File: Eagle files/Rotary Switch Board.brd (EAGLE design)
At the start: 25.4 x 25.4 mm, 0 parts

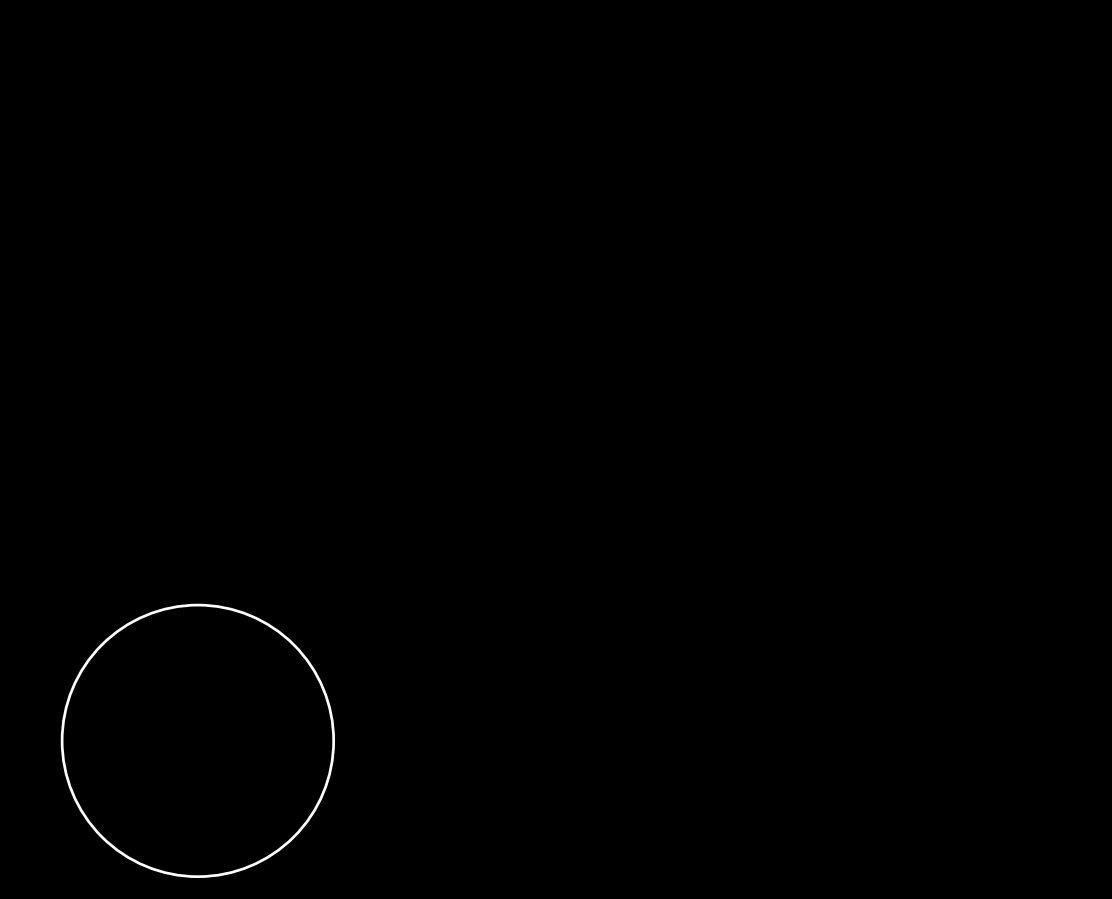
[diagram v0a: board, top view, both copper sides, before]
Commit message: Removed Rotary switch board file
Not working with OSHpark. Will troubleshoot later.
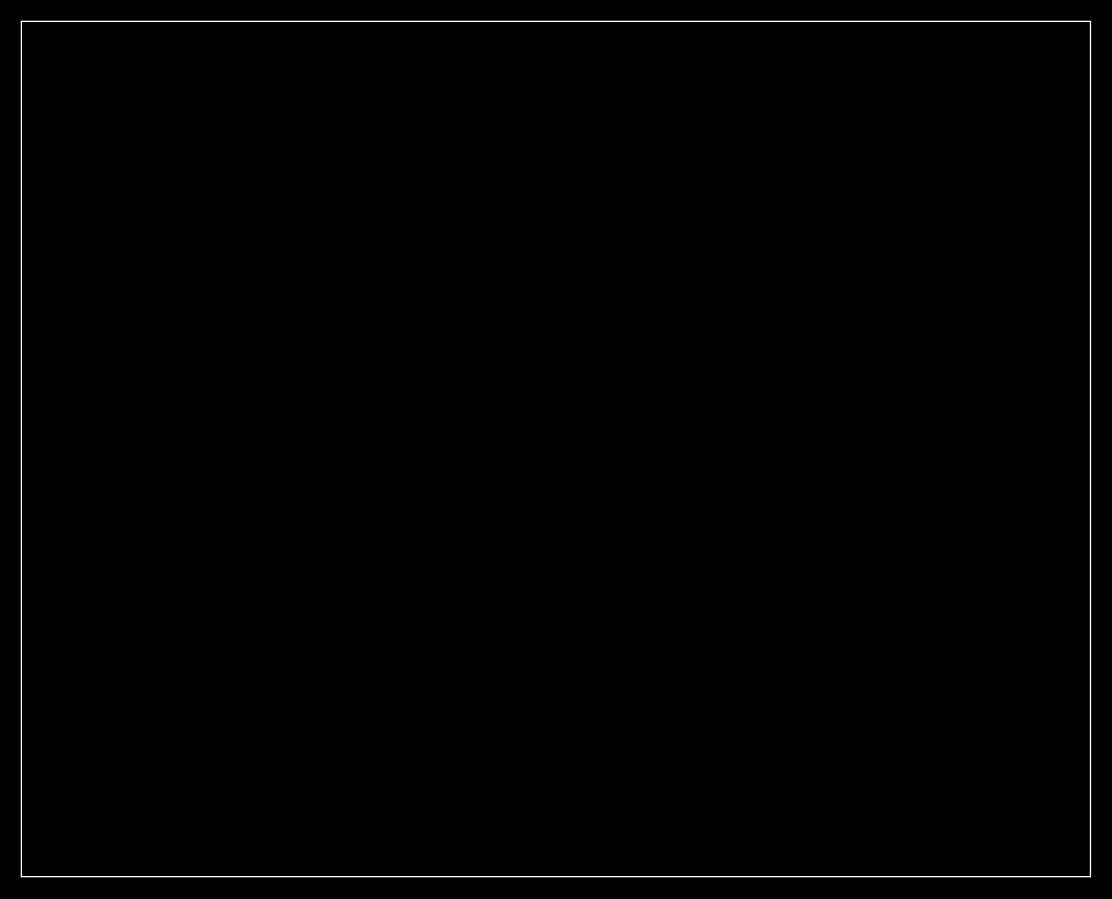
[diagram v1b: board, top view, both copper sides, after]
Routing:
- removed copper zone on layer 16, net GND
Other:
- board size 25.4 x 25.4 mm -> 100 x 80 mm
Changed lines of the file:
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@@
 <layer number="27" name="tValues" color="7" fill="1" visible="yes" active="yes"/>
 <layer number="28" name="bValues" color="7" fill="1" visible="yes" active="yes"/>
-<layer number="29" name="tStop" color="7" fill="3" visible="yes" active="yes"/>
-<layer number="30" name="bStop" color="7" fill="6" visible="yes" active="yes"/>
-<layer number="31" name="tCream" color="7" fill="4" visible="yes" active="yes"/>
-<layer number="32" name="bCream" color="7" fill="5" visible="yes" active="yes"/>
-<layer number="33" name="tFinish" color="6" fill="3" visible="yes" active="yes"/>
-<layer number="34" name="bFinish" color="6" fill="6" visible="yes" active="yes"/>
-<layer number="35" name="tGlue" color="7" fill="4" visible="yes" active="yes"/>
-<layer number="36" name="bGlue" color="7" fill="5" visible="yes" active="yes"/>
-<layer number="37" name="tTest" color="7" fill="1" visible="yes" active="yes"/>
-<layer number="38" name="bTest" color="7" fill="1" visible="yes" active="yes"/>
+<layer number="29" name="tStop" color="7" fill="3" visible="no" active="yes"/>
+<layer number="30" name="bStop" color="7" fill="6" visible="no" active="yes"/>
+<layer number="31" name="tCream" color="7" fill="4" visible="no" active="yes"/>
+<layer number="32" name="bCream" color="7" fill="5" visible="no" active="yes"/>
+<layer number="33" name="tFinish" color="6" fill="3" visible="no" active="yes"/>
+<layer number="34" name="bFinish" color="6" fill="6" visible="no" active="yes"/>
+<layer number="35" name="tGlue" color="7" fill="4" visible="no" active="yes"/>
+<layer number="36" name="bGlue" color="7" fill="5" visible="no" active="yes"/>
+<layer number="37" name="tTest" color="7" fill="1" visible="no" active="yes"/>
+<layer number="38" name="bTest" color="7" fill="1" visible="no" active="yes"/>
 <layer number="39" name="tKeepout" color="4" fill="11" visible="yes" active="yes"/>
 <layer number="40" name="bKeepout" color="1" fill="11" visible="yes" active="yes"/>
@@
 <layer number="42" name="bRestrict" color="1" fill="10" visible="yes" active="yes"/>
 <layer number="43" name="vRestrict" color="2" fill="10" visible="yes" active="yes"/>
-<layer number="44" name="Drills" color="7" fill="1" visible="yes" active="yes"/>
-<layer number="45" name="Holes" color="7" fill="1" visible="yes" active="yes"/>
-<layer number="46" name="Milling" color="3" fill="1" visible="yes" active="yes"/>
-<layer number="47" name="Measures" color="7" fill="1" visible="yes" active="yes"/>
+<layer number="44" name="Drills" color="7" fill="1" visible="no" active="yes"/>
+<layer number="45" name="Holes" color="7" fill="1" visible="no" active="yes"/>
+<layer number="46" name="Milling" color="3" fill="1" visible="no" active="yes"/>
+<layer number="47" name="Measures" color="7" fill="1" visible="no" active="yes"/>
 <layer number="48" name="Document" color="7" fill="1" visible="yes" active="yes"/>
 <layer number="49" name="Reference" color="7" fill="1" visible="yes" active="yes"/>
@@
 <board>
 <plain>
-<circle x="16.51" y="12.7" radius="12.7" width="0.254" layer="20"/>
+<wire x1="0" y1="0" x2="100" y2="0" width="0" layer="20"/>
+<wire x1="100" y1="0" x2="100" y2="80" width="0" layer="20"/>
+<wire x1="100" y1="80" x2="0" y2="80" width="0" layer="20"/>
+<wire x1="0" y1="80" x2="0" y2="0" width="0" layer="20"/>
 </plain>
 <attributes>
@@
 </elements>
 <signals>
-<signal name="GND">
-<polygon width="0" layer="16">
-<vertex x="29.21" y="12.7" curve="-90"/>
-<vertex x="16.51" y="0" curve="-90"/>
-<vertex x="3.81" y="12.7" curve="-90"/>
-<vertex x="16.51" y="25.4" curve="-90"/>
-</polygon>
-</signal>
 </signals>
 </board>
